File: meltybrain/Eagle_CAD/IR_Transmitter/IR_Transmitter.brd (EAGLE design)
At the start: 33.2 x 27.6 mm, 14 parts, among them J1 AVR_SPI_PROG_3X2NS, Q1 BSS806N, Q2 FDN352AP, U1 LMH6612MAX/NOPB, U2 AP2210K-5.0TRG1

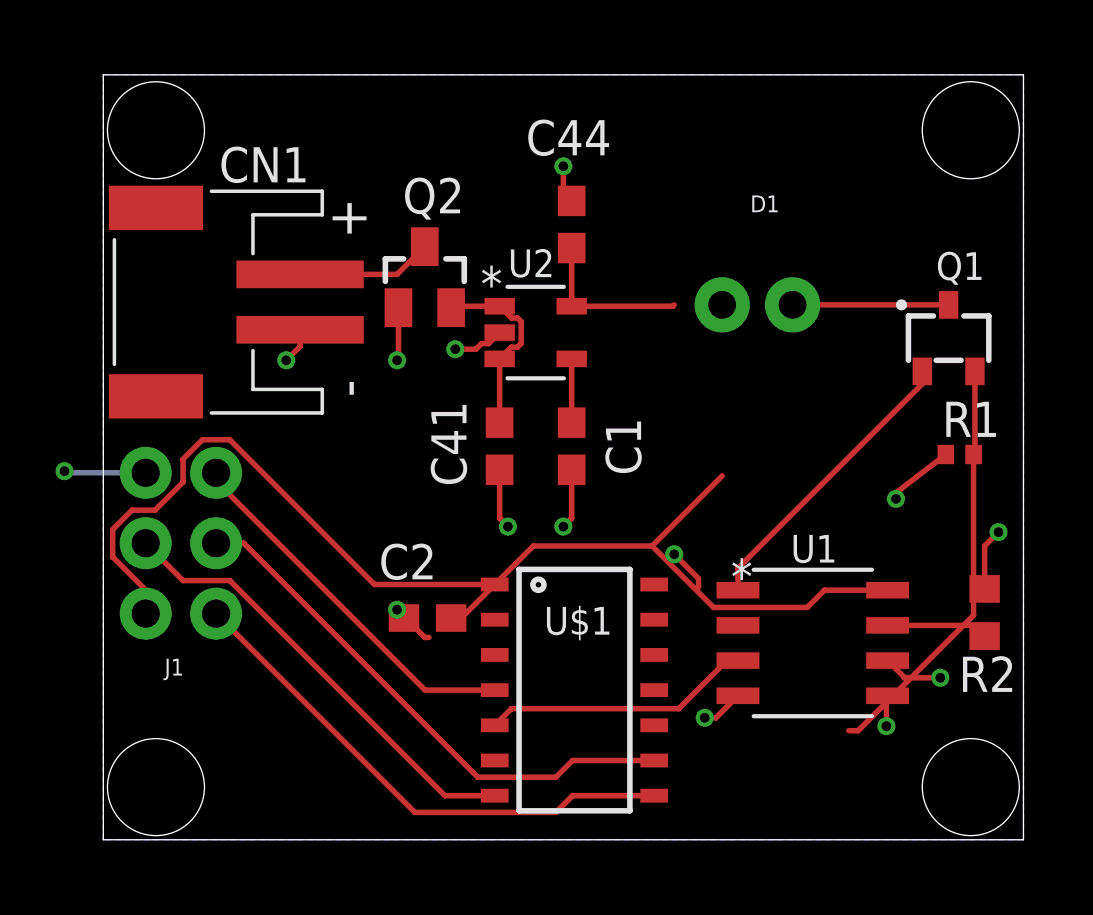
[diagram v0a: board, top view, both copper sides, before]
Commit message: Updated Hocki IR Receiver and removed extraneous file
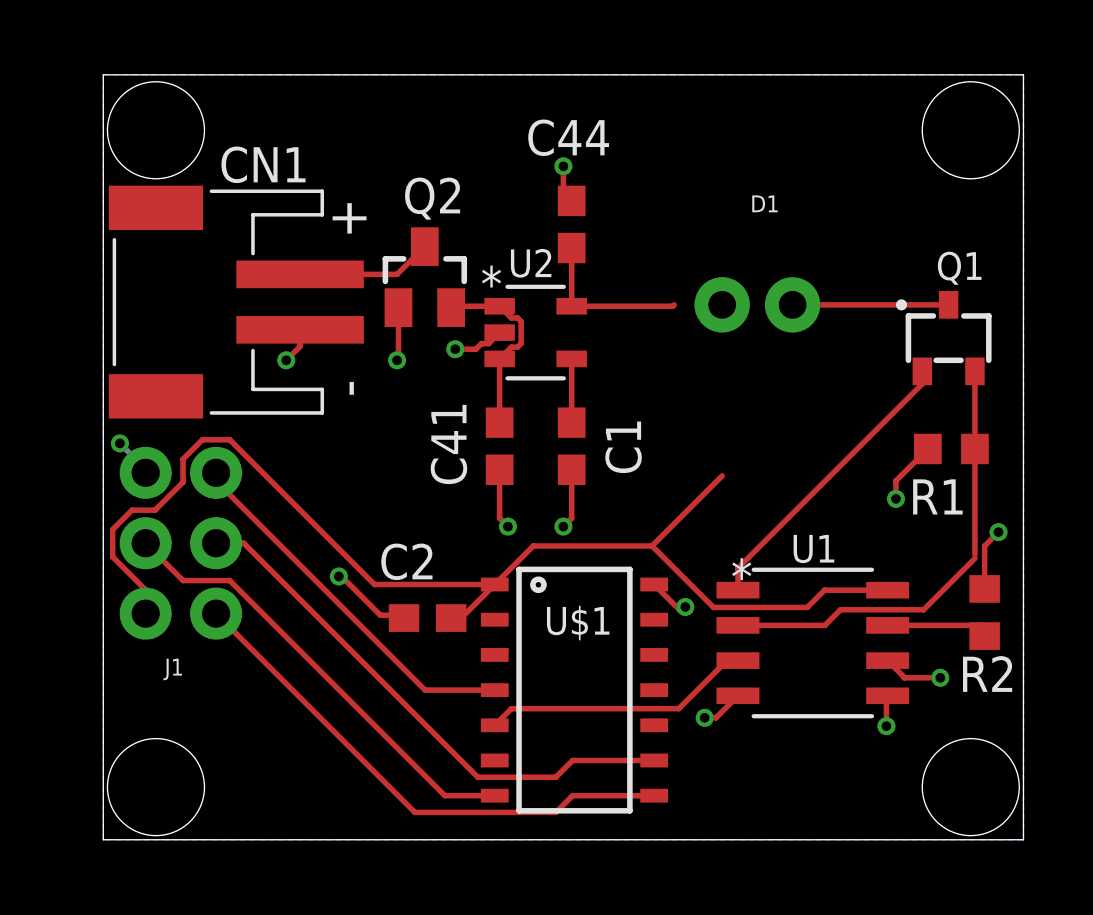
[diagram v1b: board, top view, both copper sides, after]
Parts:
- R1: value 1.5 -> 6.8; device rcl:R0402 -> rcl:R0603
- moved R1 0.36 mm to (32.0, 14.8)
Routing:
- net N$1: track 15.0 -> 16.3 mm
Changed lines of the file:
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@@
 <attribute name="VALUE" x="25" y="4.8" size="1" layer="27" font="vector" rot="SR0" align="top-left"/>
 </element>
-<element name="R1" library="rcl" library_urn="urn:adsk.eagle:library:334" package="R0402" package3d_urn="urn:adsk.eagle:package:23547/3" value="1.5" x="32.3" y="14.6" smashed="yes">
-<attribute name="NAME" x="31.665" y="15.235" size="1.27" layer="25"/>
-<attribute name="POPULARITY" value="34" x="32.3" y="14.6" size="1.778" layer="27" display="off"/>
-<attribute name="SPICEPREFIX" value="R" x="32.3" y="14.6" size="1.778" layer="27" display="off"/>
-<attribute name="VALUE" x="31.665" y="12.695" size="1.27" layer="27"/>
+<element name="R1" library="rcl" library_urn="urn:adsk.eagle:library:334" package="R0603" package3d_urn="urn:adsk.eagle:package:23555/3" value="6.8" x="32" y="14.8" smashed="yes">
+<attribute name="NAME" x="30.465" y="12.435" size="1.27" layer="25"/>
+<attribute name="POPULARITY" value="77" x="32" y="14.8" size="1.778" layer="27" display="off"/>
+<attribute name="SPICEPREFIX" value="R" x="32" y="14.8" size="1.778" layer="27" display="off"/>
+<attribute name="VALUE" x="31.365" y="12.895" size="1.27" layer="27"/>
 </element>
 <element name="R2" library="rcl" library_urn="urn:adsk.eagle:library:334" package="R0603" package3d_urn="urn:adsk.eagle:package:23555/3" value="500" x="33.2" y="8.9" smashed="yes" rot="R270">
@@
 <contactref element="Q1" pad="2"/>
 <contactref element="R1" pad="2"/>
-<wire x1="28.635" y1="4.635" x2="28.3" y2="4.635" width="0.2" layer="1"/>
-<wire x1="32" y1="8" x2="28.635" y2="4.635" width="0.2" layer="1"/>
-<wire x1="32.85" y1="17.6" x2="32.85" y2="14.65" width="0.2" layer="1"/>
-<wire x1="32.85" y1="14.65" x2="32.8" y2="14.6" width="0.2" layer="1"/>
-<wire x1="32.8" y1="14.6" x2="32.8" y2="8.8" width="0.2" layer="1"/>
-<wire x1="32.8" y1="8.8" x2="32" y2="8" width="0.2" layer="1"/>
+<wire x1="32.85" y1="17.6" x2="32.85" y2="14.8" width="0.2" layer="1"/>
+<wire x1="32.85" y1="14.8" x2="32.85" y2="11" width="0.2" layer="1"/>
+<wire x1="24.3" y1="8.435" x2="27.435" y2="8.435" width="0.2" layer="1"/>
+<wire x1="27.435" y1="8.435" x2="28" y2="9" width="0.2" layer="1"/>
+<wire x1="31" y1="9" x2="28" y2="9" width="0.2" layer="1"/>
+<wire x1="32.85" y1="11" x2="32.85" y2="10.85" width="0.1524" layer="1"/>
+<wire x1="31" y1="9" x2="32.85" y2="10.85" width="0.2" layer="1"/>
 </signal>
 <signal name="N$2">
@@
 <wire x1="18.3" y1="12.3" x2="18" y2="12" width="0.2" layer="1"/>
 <via x="18" y="12" extent="1-16" drill="0.35"/>
-<wire x1="22.875" y1="9.81" x2="22.875" y2="10.125" width="0.2" layer="1"/>
-<wire x1="22.875" y1="10.125" x2="22" y2="11" width="0.2" layer="1"/>
-<via x="22" y="11" extent="1-16" drill="0.35"/>
-<wire x1="13.15" y1="8" x2="13" y2="8" width="0.2" layer="1"/>
-<wire x1="13" y1="8" x2="12" y2="9" width="0.2" layer="1"/>
-<via x="12" y="9" extent="1-16" drill="0.35"/>
-<wire x1="2.93" y1="13.94" x2="0.06" y2="13.94" width="0.2" layer="16"/>
-<wire x1="0.06" y1="13.94" x2="0" y2="14" width="0.2" layer="16"/>
-<via x="0" y="14" extent="1-16" drill="0.35"/>
-<wire x1="31.8" y1="14.6" x2="30" y2="13.22" width="0.2" layer="1"/>
-<wire x1="30" y1="13.22" x2="30" y2="13" width="0.2" layer="1"/>
+<wire x1="22.4" y1="9.1" x2="22.290003125" y2="9.1" width="0.2" layer="1"/>
+<wire x1="22.290003125" y1="9.1" x2="22.2" y2="9.01" width="0.2" layer="1"/>
+<wire x1="22.2" y1="9.01" x2="22.175" y2="9.01" width="0.2" layer="1"/>
+<wire x1="21.275" y1="9.91" x2="22.175" y2="9.01" width="0.2" layer="1"/>
+<via x="22.4" y="9.1" extent="1-16" drill="0.35"/>
+<wire x1="12.25" y1="8.7" x2="12.15" y2="8.8" width="0.2" layer="1"/>
+<wire x1="12.15" y1="8.8" x2="11.4" y2="8.8" width="0.2" layer="1"/>
+<wire x1="11.4" y1="8.8" x2="10" y2="10.2" width="0.2" layer="1"/>
+<wire x1="9.9" y1="10.2" x2="10" y2="10.2" width="0.2" layer="1"/>
+<via x="9.9" y="10.2" extent="1-16" drill="0.35"/>
+<wire x1="2.93" y1="13.94" x2="2.93" y2="14.07" width="0.2" layer="16"/>
+<wire x1="2.93" y1="14.07" x2="2" y2="15" width="0.2" layer="16"/>
+<via x="2" y="15" extent="1-16" drill="0.35"/>
+<wire x1="31.15" y1="14.8" x2="30" y2="13.65" width="0.2" layer="1"/>
+<wire x1="30" y1="13.65" x2="30" y2="13" width="0.2" layer="1"/>
 <via x="30" y="13" extent="1-16" drill="0.35"/>
 <wire x1="33.7" y1="11.8" x2="33.2" y2="11.3" width="0.2" layer="1"/>

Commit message: Finalized emitter board
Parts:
- removed U$1: ATTINY84, EmitterParts:SOIC-14
- added U3: ATTINY84, EmitterParts:SOIC-14
- R1: value 6.8 -> 1.5; device rcl:R0603 -> rcl:R0402
- moved Q1 10.2 mm to (23.5, 13.1)
- moved R1 6.82 mm to (26.4, 10.9), turned to 180 degrees
- moved U1 5.10 mm to (21.9, 8.00)
- moved C2 4.92 mm to (10.7, 13.0)
- moved R2 4.41 mm to (28.8, 9.20)
- moved D1 2.98 mm to (22.7, 18.1)
- moved CN1 2.52 mm to (3.40, 18.0)
- moved J1 2.28 mm to (5.60, 9.60), turned to 0 degrees
- moved C1 1.57 mm to (16.9, 14.2)
- moved C44 1.57 mm to (16.9, 22.2)
- moved Q2 1.57 mm to (11.6, 20.3)
- moved U2 1.57 mm to (15.6, 18.3)
- moved C41 1.57 mm to (14.3, 14.2)
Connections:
- net +5V: now also U3.1; no longer U$1.1
- net GND: now also U3.14; no longer U$1.14
- net MISO: now also U3.8; no longer U$1.8
- net MOSI: now also U3.7; no longer U$1.7
- net OUT: now also U3.5; no longer U$1.5
- net RST: now also U3.4; no longer U$1.4
- net SCK: now also U3.9; no longer U$1.9
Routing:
- net RST: track 13.5 -> 4.20 mm
- net N$2: track 10.6 -> 4.18 mm
- net N$1: track 16.3 -> 10.1 mm
- net GND: track 26.2 -> 20.5 mm, vias 14 -> 13
- net +5V: track 48.7 -> 44.1 mm
- net SCK: track 19.6 -> 15.2 mm
- net MOSI: track 16.4 -> 13.5 mm
- net N$5: track 5.63 -> 3.99 mm
- net MISO: track 19.0 -> 17.5 mm
- net N$3: track 3.88 -> 4.48 mm
- net 9V: track 4.91 -> 5.49 mm
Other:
- board size 33.2 x 27.6 mm -> 30.9 x 28.5 mm

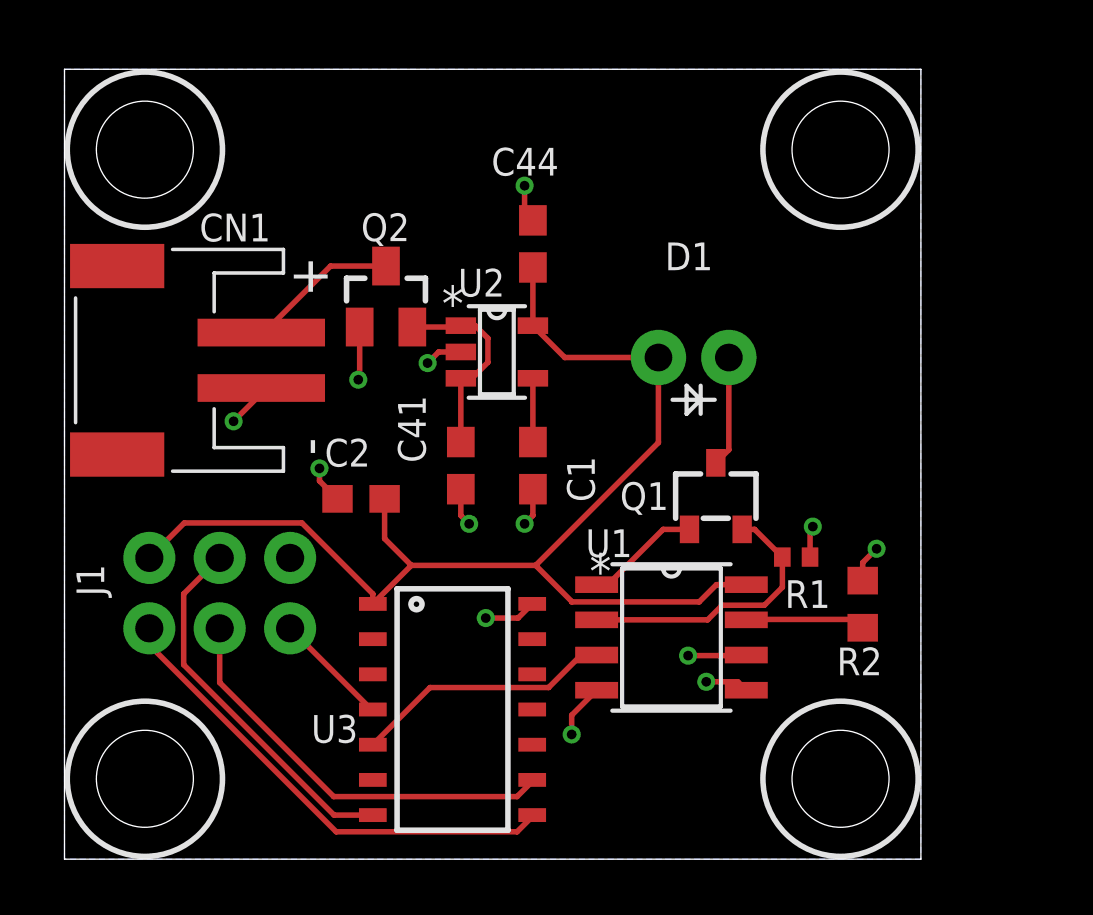
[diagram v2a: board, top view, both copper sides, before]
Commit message: Updated 3D CAD models
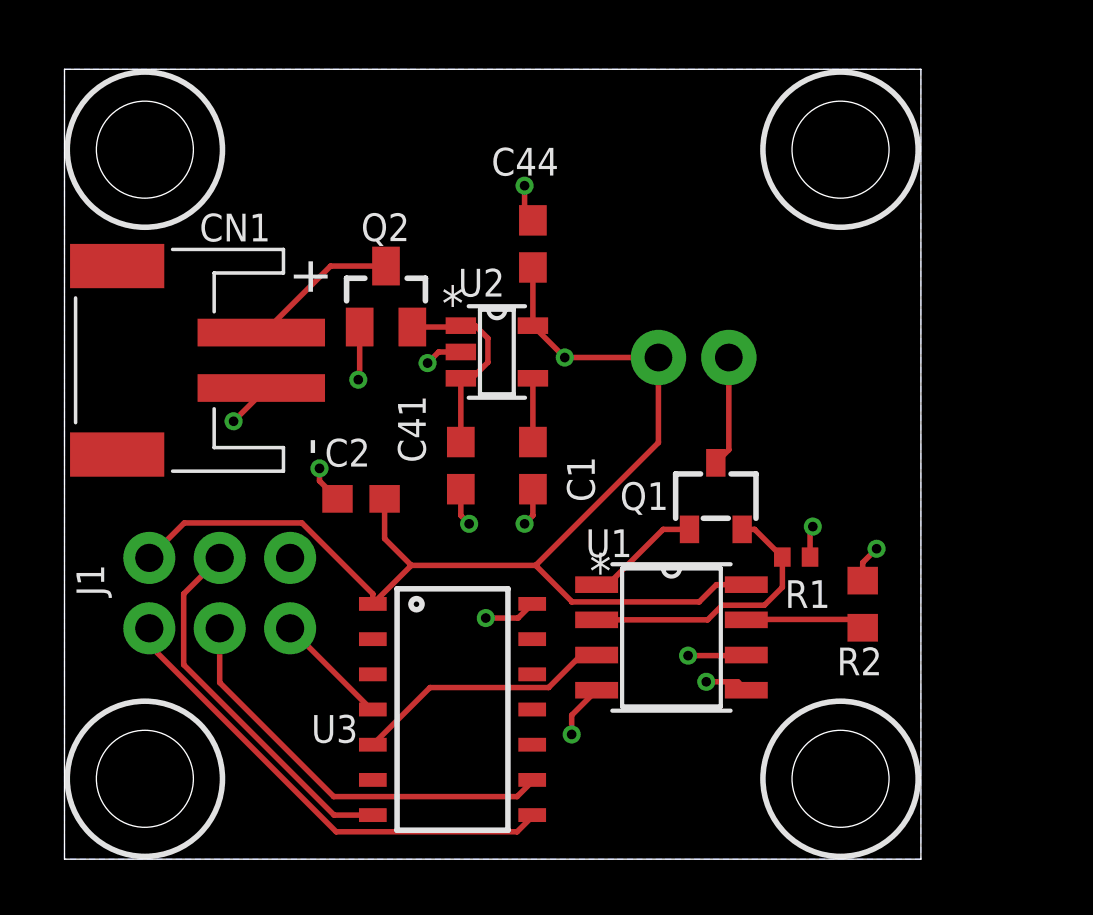
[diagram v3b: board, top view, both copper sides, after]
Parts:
- flipped D1 to the bottom, turned to 0 degrees
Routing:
- net +5V: vias 0 -> 1
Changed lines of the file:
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@@
 <?xml version="1.0" encoding="utf-8"?>
 <!DOCTYPE eagle SYSTEM "eagle.dtd">
-<eagle version="9.6.2">
+<eagle version="9.5.2">
 <drawing>
 <settings>
@@
 <setting verticaltext="up"/>
 </settings>
-<grid distance="1" unitdist="mm" unit="mm" style="lines" multiple="1" display="no" altdistance="0.1" altunitdist="mm" altunit="mm"/>
+<grid distance="0.01" unitdist="mm" unit="mm" style="lines" multiple="1" display="no" altdistance="0.1" altunitdist="mm" altunit="mm"/>
 <layers>
 <layer number="1" name="Top" color="4" fill="1" visible="yes" active="yes"/>
@@
 </layers>
 <board>
+<fusionsync huburn="a.cGVyc29uYWw6dWUyY2EyMWFk" projecturn="a.cGVyc29uYWw6dWUyZDhlY2M3IzIwMjAwNzEyMzE1MDc1MjU2" f3durn="urn:adsk.wipprod:dm.lineage:YGfndywUS02_83q7guT35Q" pcbguid="3c4bd254-c4ce-4655-8dd0-7a827ae63bfb" lastpulledtime="" lastsyncedchangeguid="a4fb0dd9-0eee-2ea1-3cea-b7b776e116ba"/>
 <plain>
 <wire x1="0" y1="0" x2="30.9" y2="0" width="0" layer="20"/>
@@
 <attribute name="VALUE" x="14.6" y="16.3" size="1" layer="27" font="vector" rot="SR0" align="top-left"/>
 </element>
-<element name="D1" library="EmitterParts" package="DIO_SFH_4544" value="SFH_4544" x="22.7" y="18.1" smashed="yes" rot="R180">
-<attribute name="DKPN" value="475-3524-ND" x="22.7" y="18.1" size="1.778" layer="27" rot="R180" display="off"/>
-<attribute name="NAME" x="23.4" y="22.25" size="1" layer="25" font="vector" ratio="10" rot="R180"/>
-<attribute name="VALUE" x="27.5" y="21.242" size="0.6096" layer="27" rot="R180" align="top-left"/>
+<element name="D1" library="EmitterParts" package="DIO_SFH_4544" override_package3d_urn="urn:adsk.eagle:package:22908895/2" override_package_urn="urn:adsk.eagle:footprint:22908896/1" value="SFH_4544" x="22.7" y="18.1" smashed="yes" rot="MR0">
+<attribute name="DKPN" value="475-3524-ND" x="22.7" y="18.1" size="1.778" layer="28" rot="MR0" display="off"/>
+<attribute name="NAME" x="23.4" y="13.95" size="1" layer="26" font="vector" ratio="10" rot="MR0"/>
+<attribute name="VALUE" x="27.5" y="14.958" size="0.6096" layer="28" rot="MR0" align="top-left"/>
 </element>
 <element name="C41" library="rcl" library_urn="urn:adsk.eagle:library:334" package="C0603" package3d_urn="urn:adsk.eagle:package:23616/2" value="1u" x="14.3" y="14.2" smashed="yes" rot="R270">
@@
 <attribute name="VALUE" x="8.826859375" y="18.096809375" size="1.27" layer="27" align="top-left"/>
 </element>
-<element name="CN1" library="Hocki_Library" package="JST-PH-2-SMT-RA" value="" x="3.4" y="18" smashed="yes" rot="R90">
+<element name="CN1" library="Hocki_Library" package="JST-PH-2-SMT-RA" override_package3d_urn="urn:adsk.eagle:package:22908887/2" override_package_urn="urn:adsk.eagle:footprint:22908888/1" value="" x="3.4" y="18" smashed="yes" rot="R90">
 <attribute name="NAME" x="7.44" y="23.29" size="1" layer="25" font="vector" ratio="10" rot="R180"/>
 <attribute name="VALUE" x="11.02" y="15.46" size="1.27" layer="27" font="vector" rot="R90"/>
 </element>
-<element name="J1" library="SparkFun-Connectors" library_urn="urn:adsk.eagle:library:513" package="2X3-NS" package3d_urn="urn:adsk.eagle:package:38013/1" value="AVR_SPI_PROG_3X2NS" x="5.6" y="9.6" smashed="yes">
+<element name="J1" library="SparkFun-Connectors" library_urn="urn:adsk.eagle:library:513" package="2X3-NS" package3d_urn="urn:adsk.eagle:package:38013/1" override_package3d_urn="urn:adsk.eagle:package:22908900/2" override_package_urn="urn:adsk.eagle:footprint:37609/1" value="AVR_SPI_PROG_3X2NS" x="5.6" y="9.6" smashed="yes">
 <attribute name="NAME" x="1.433" y="9.49" size="1" layer="25" font="vector" ratio="10" rot="R90"/>
 <attribute name="VALUE" x="1.79" y="5.663" size="0.6096" layer="27" font="vector" ratio="20"/>
@@
 <wire x1="8.56383125" y1="12.1322" x2="11.125" y2="9.57103125" width="0.2" layer="1"/>
 <wire x1="12.515" y1="10.6" x2="17" y2="10.6" width="0.2" layer="1"/>
-<wire x1="17" y1="10.6" x2="21.43" y2="15.03" width="0.2" layer="1"/>
+<wire x1="21.43" y1="15.03" x2="17" y2="10.6" width="0.2" layer="1"/>
 <wire x1="16.9" y1="21.35" x2="16.9" y2="19.25" width="0.2" layer="1"/>
 <contactref element="C2" pad="1"/>
@@
 <wire x1="22.9" y1="9.2826" x2="23.5224" y2="9.905" width="0.2" layer="1"/>
 <contactref element="D1" pad="A"/>
-<wire x1="21.43" y1="15.03" x2="21.43" y2="18.1" width="0.2" layer="1"/>
-<wire x1="21.43" y1="18.1" x2="18.05" y2="18.1" width="0.2" layer="1"/>
 <wire x1="16.9" y1="19.25" x2="18.05" y2="18.1" width="0.2" layer="1"/>
 <wire x1="18.3" y1="9.2826" x2="22.9" y2="9.2826" width="0.2" layer="1"/>
@@
 <wire x1="17" y1="10.6" x2="18.3" y2="9.3" width="0.2" layer="1"/>
 <wire x1="18.3" y1="9.3" x2="18.3" y2="9.2826" width="0.2" layer="1"/>
+<via x="18.05" y="18.1" extent="1-16" drill="0.35"/>
+<wire x1="18.05" y1="18.1" x2="21.43" y2="18.1" width="0.2" layer="1"/>
+<wire x1="21.43" y1="18.1" x2="21.43" y2="15.03" width="0.2" layer="1"/>
 </signal>
 <signal name="N$5">
@@
 </note>
 <note version="8.3" severity="warning">
+Since Version 8.3, EAGLE supports Fusion synchronisation.
+This feature will not be available in this version and saving
+the document will break the link to the Fusion PCB feature.
+</note>
+<note version="8.3" severity="warning">
 Since Version 8.3, EAGLE supports URNs for individual library
 assets (packages, symbols, and devices). The URNs of those assets
@@
 packages will not be understood (or retained) with this version.
 </note>
+<note version="9.4" severity="warning">
+Since Version 9.4, EAGLE supports the overriding of 3D packages
+in schematics and board files. Those overridden 3d packages
+will not be understood (or retained) with this version.
+</note>
 </compatibility>

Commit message: second round of gerbers
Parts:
- R1: device rcl:R0402 -> rcl:R0805
- moved R1 2.10 mm to (26.4, 13.0), turned to 270 degrees
- moved R2 2.00 mm to (26.8, 9.20)
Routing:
- net +5V: track 44.1 -> 0.00 mm, vias 1 -> 0
- net GND: track 20.5 -> 16.9 mm
- net N$3: track 4.48 -> 2.48 mm
- net N$1: track 10.1 -> 8.61 mm
- net RST: track 4.20 -> 4.90 mm
- added copper zone on layer 1, net +5V
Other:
- board size 30.9 x 28.5 mm -> 31 x 29 mm
